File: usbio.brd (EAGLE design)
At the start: 12.3 x 40.1 mm, 20 parts, among them U1 ATMEGA328P-MU-QFN32

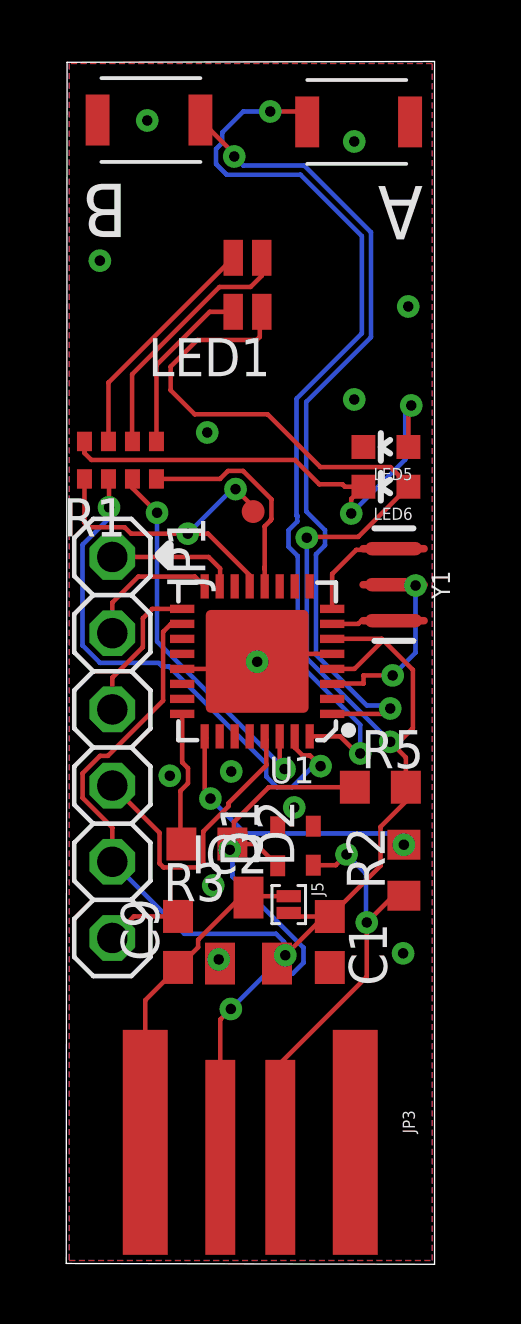
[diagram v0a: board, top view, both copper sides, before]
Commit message: Narrow sides to fit usb 12mm width constraint
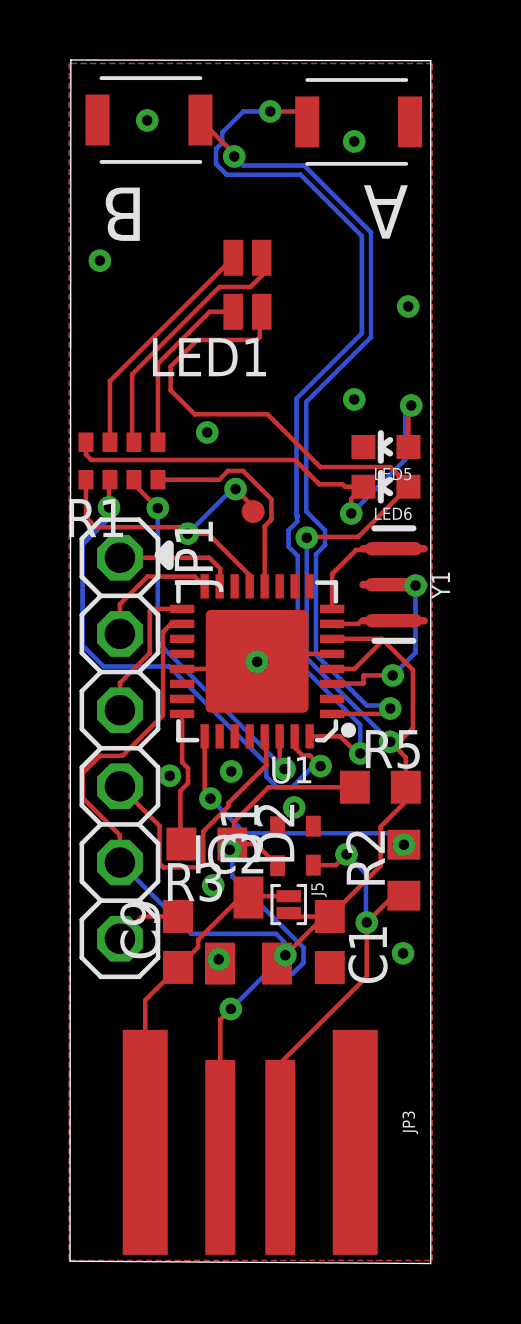
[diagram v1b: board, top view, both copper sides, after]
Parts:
- moved JP1 0.26 mm to (1.79, 17.2)
- moved R1 0.06 mm to (1.86, 26.8)
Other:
- board size 12.3 x 40.1 mm -> 12 x 40.1 mm

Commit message: Optimize vias
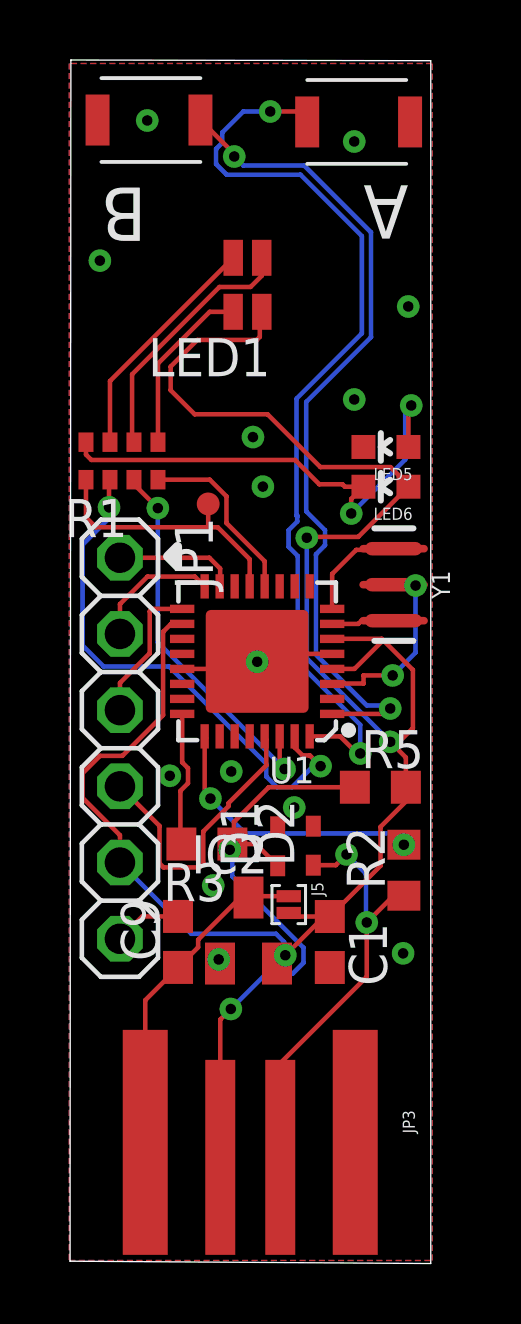
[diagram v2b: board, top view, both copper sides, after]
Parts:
- moved TP1 1.52 mm to (4.73, 25.3)
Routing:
- net ADCENA: track 11.1 -> 9.54 mm, vias 2 -> 0
- net LED: track 7.29 -> 6.04 mm
- net GND: vias 15 -> 16
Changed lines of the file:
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@@
 <circle x="5.9436" y="32.5374" radius="0.534003125" width="1.27" layer="30"/>
 <polygon width="0.3048" layer="21">
-<vertex x="3.0988" y="23.622"/>
-<vertex x="3.429" y="23.9522"/>
-<vertex x="3.429" y="23.2664"/>
-<vertex x="3.0988" y="23.5966"/>
+<vertex x="3.3782" y="23.5712"/>
+<vertex x="3.7084" y="23.9014"/>
+<vertex x="3.7084" y="23.241"/>
 </polygon>
 </plain>
@@
 <attribute name="VALUE" x="9.835" y="13.97" size="1.27" layer="27"/>
 </element>
-<element name="TP1" library="SparkFun" package="PAD.03X.03" value="TEST-POINT3" x="6.23" y="25.064" smashed="yes"/>
+<element name="TP1" library="SparkFun" package="PAD.03X.03" value="TEST-POINT3" x="4.7314" y="25.318" smashed="yes"/>
 <element name="U$2" library="pusbbutton_4x2_5" package="PUSHBUTTON_4X2.5" value="PUSHBUTTON_4X2.5" x="9.302" y="38.052" smashed="yes"/>
 <element name="U$3" library="pusbbutton_4x2_5" package="PUSHBUTTON_4X2.5" value="PUSHBUTTON_4X2.5" x="3.203" y="38.115" smashed="yes" rot="R180"/>
@@
 <via x="11.4" y="31.9" extent="1-16" drill="0.35"/>
 <via x="9.6" y="28.8" extent="1-16" drill="0.35"/>
-<via x="4.7" y="27.7" extent="1-16" drill="0.35"/>
+<via x="6.224" y="27.5476" extent="1-16" drill="0.35"/>
 <via x="1.1206" y="33.4284" extent="1-16" drill="0.35"/>
 <via x="9.6" y="37.4" extent="1-16" drill="0.35"/>
@@
 <via x="3.4522" y="16.2576" extent="1-16" drill="0.35"/>
 <via x="5.0818" y="10.135" extent="1-16" drill="0.35"/>
+<via x="6.5542" y="25.8966" extent="1-16" drill="0.35"/>
 </signal>
 <signal name="LED">
 <contactref element="R1" pad="4"/>
 <contactref element="U1" pad="12"/>
-<wire x1="3.0578" y1="26.1266" x2="5.09945" y2="26.1266" width="0.1524" layer="1"/>
-<wire x1="5.09945" y1="26.1266" x2="5.39165" y2="26.4188" width="0.1524" layer="1"/>
-<wire x1="5.39165" y1="26.4188" x2="5.89435" y2="26.4188" width="0.1524" layer="1"/>
-<wire x1="6.8396" y1="24.81149375" x2="6.8072" y2="24.77909375" width="0.1524" layer="1"/>
-<wire x1="6.8072" y1="24.77909375" x2="6.8072" y2="24.765" width="0.1524" layer="1"/>
-<wire x1="5.89435" y1="26.4188" x2="6.8396" y2="25.47355" width="0.1524" layer="1"/>
-<wire x1="6.8396" y1="25.47355" x2="6.8396" y2="24.81149375" width="0.1524" layer="1"/>
-<wire x1="6.8072" y1="24.765" x2="6.614" y2="24.5718" width="0.1524" layer="1"/>
-<wire x1="6.614" y1="24.5718" x2="6.614" y2="22.57" width="0.1524" layer="1"/>
+<wire x1="5.341" y1="25.57050625" x2="5.341" y2="24.68105625" width="0.1524" layer="1"/>
+<wire x1="4.78490625" y1="26.1266" x2="5.341" y2="25.57050625" width="0.1524" layer="1"/>
+<wire x1="3.0578" y1="26.1266" x2="4.78490625" y2="26.1266" width="0.1524" layer="1"/>
+<wire x1="6.614" y1="23.40805625" x2="6.614" y2="22.57" width="0.1524" layer="1"/>
+<wire x1="5.341" y1="24.68105625" x2="6.614" y2="23.40805625" width="0.1524" layer="1"/>
 </signal>
 <signal name="+3V3">
@@
 <wire x1="6.114" y1="22.57" x2="6.1093" y2="22.5747" width="0.1524" layer="1"/>
 <wire x1="6.1093" y1="22.5747" x2="6.1093" y2="22.9440875" width="0.1524" layer="1"/>
-<wire x1="6.1093" y1="22.9440875" x2="4.7263875" y2="24.327" width="0.1524" layer="1"/>
-<wire x1="4.7263875" y1="24.327" x2="4.05" y2="24.327" width="0.1524" layer="1"/>
-<via x="4.05" y="24.327" extent="1-16" drill="0.35"/>
-<wire x1="4.05" y1="24.327" x2="5.508" y2="25.785" width="0.1524" layer="16"/>
-<wire x1="5.508" y1="25.785" x2="5.643" y2="25.785" width="0.1524" layer="16"/>
-<wire x1="5.643" y1="25.785" x2="5.643" y2="25.812" width="0.1524" layer="16"/>
-<via x="5.643" y="25.812" extent="1-16" drill="0.35"/>
-<wire x1="5.643" y1="25.812" x2="6.23" y2="25.225" width="0.1524" layer="1"/>
-<wire x1="6.23" y1="25.225" x2="6.23" y2="25.064" width="0.1524" layer="1"/>
-<wire x1="0.987" y1="24.5406" x2="0.6578" y2="24.8698" width="0.1524" layer="1"/>
+<wire x1="4.7314" y1="25.479" x2="4.7314" y2="25.318" width="0.1524" layer="1"/>
+<wire x1="0.6578" y1="24.8698" x2="0.987" y2="24.5406" width="0.1524" layer="1"/>
 <wire x1="0.6578" y1="24.8698" x2="0.6578" y2="26.1266" width="0.1524" layer="1"/>
-<wire x1="4.05" y1="24.327" x2="3.8364" y2="24.5406" width="0.1524" layer="1"/>
-<wire x1="3.8364" y1="24.5406" x2="0.987" y2="24.5406" width="0.1524" layer="1"/>
+<wire x1="6.114" y1="22.57" x2="6.114" y2="23.477" width="0.1524" layer="1"/>
+<wire x1="6.114" y1="23.477" x2="5.0504" y2="24.5406" width="0.1524" layer="1"/>
+<wire x1="5.0504" y1="24.5406" x2="4.8006" y2="24.5406" width="0.1524" layer="1"/>
+<wire x1="4.8006" y1="24.5406" x2="0.987" y2="24.5406" width="0.1524" layer="1"/>
+<wire x1="4.7314" y1="25.318" x2="4.7314" y2="24.6098" width="0.1524" layer="1"/>
+<wire x1="4.7314" y1="24.6098" x2="4.8006" y2="24.5406" width="0.1524" layer="1"/>
 </signal>
 <signal name="TXD">
